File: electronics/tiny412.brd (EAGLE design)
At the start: 18.8 x 16.3 mm, 25 parts

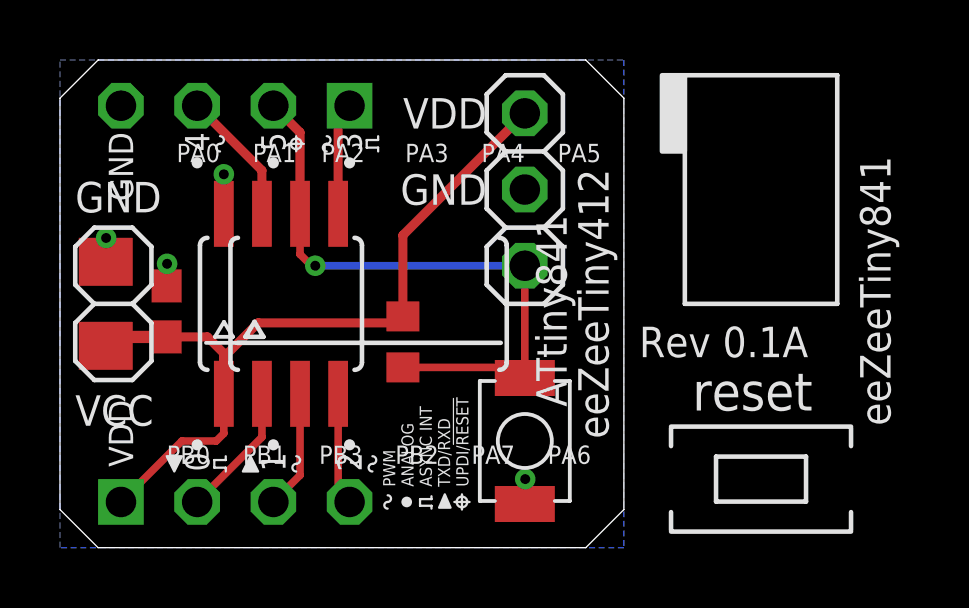
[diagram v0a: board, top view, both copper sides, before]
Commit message: Updated silk symbols, enlarged; fixed reset ckt, added HF filter cap
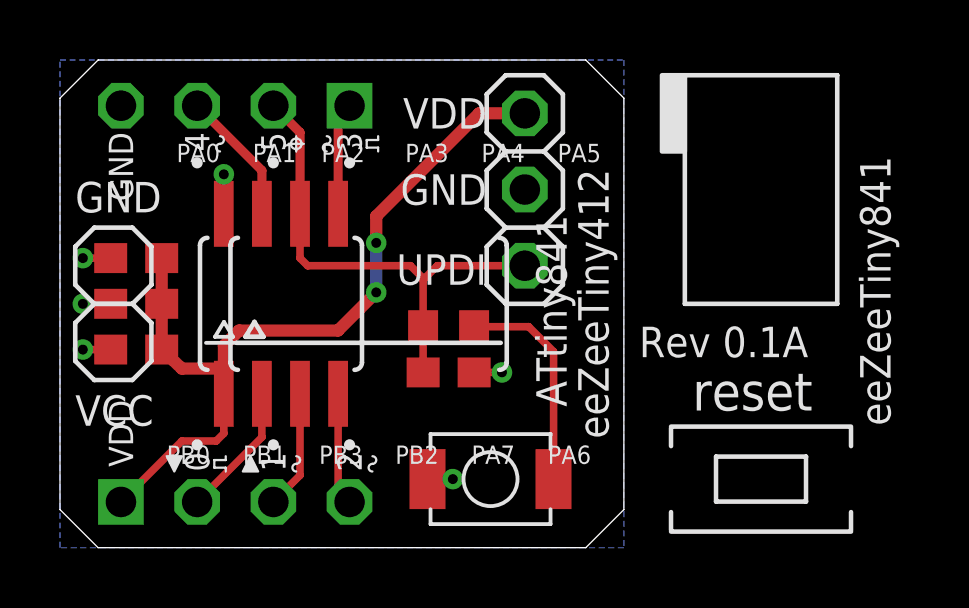
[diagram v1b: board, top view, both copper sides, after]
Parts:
- removed R1: 10k, rcl:R0603
- added C3: 102, rcl:C0603
- added C4: 104, rcl:C0603
- added R2: 330, rcl:R0603
- C2: device bt_rcl:1206 -> bt_rcl:0603
- S1: value RST -> RESET
- moved U$10 5.64 mm to (17.4, 4.19), flipped to the bottom, turned to 0 degrees
- moved C2 1.83 mm to (2.54, 9.65), turned to 180 degrees
- moved U$1 1.78 mm to (5.84, 6.73)
- moved S1 1.71 mm to (14.4, 2.29), turned to 0 degrees
- moved C1 1.63 mm to (2.54, 6.60), turned to 180 degrees
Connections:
- new net N$1: R2.1, S1.P$2
- net !RESET: now also C4.1, R2.2; no longer R1.1, S1.P$2
- net GND: now also C3.2, C4.2
- net VCC: now also C3.1; no longer R1.2
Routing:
- net N$1: track 0.00 -> 7.24 mm
- net !RESET: track 21.0 -> 16.6 mm, vias 1 -> 0
- net GND: track 3.68 -> 5.87 mm, vias 4 -> 6
- net VCC: track 28.1 -> 27.4 mm, vias 0 -> 2
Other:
- board text added: "R0.2"
- board text added: "cc-by-sa"
- board text removed: "CC-BY-SA"
- board text removed: "R0.1"

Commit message: remove reset, updated pin desc, added doc url
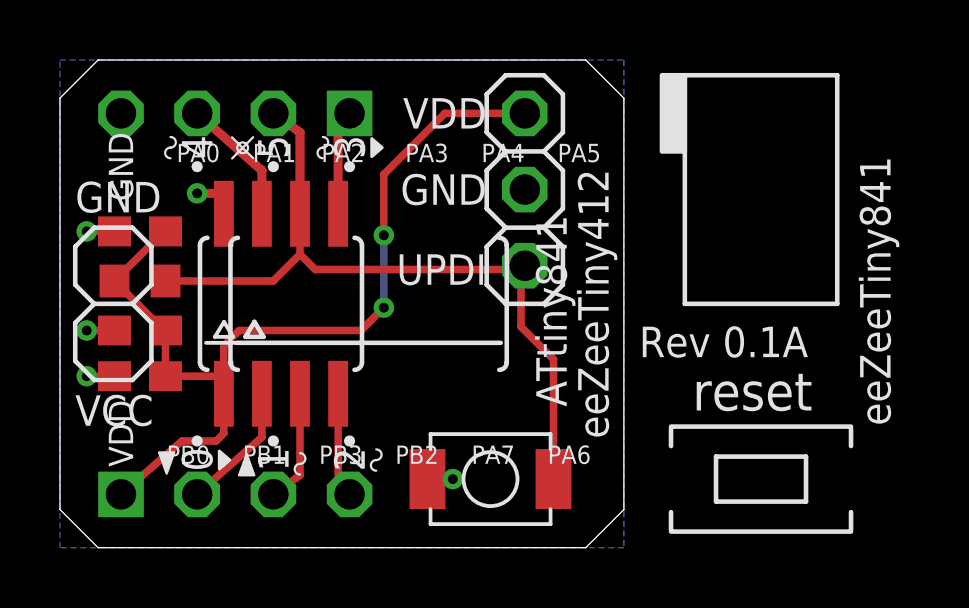
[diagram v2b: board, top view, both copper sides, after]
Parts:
- removed C4: 104, rcl:C0603
- R2: value 330 -> 10k
- moved R2 10.4 mm to (2.67, 8.89)
- moved U$11 1.78 mm to (6.10, 13.3)
- moved U$3 1.66 mm to (3.68, 13.3)
- moved C2 0.90 mm to (2.67, 10.5)
- moved C1 0.90 mm to (2.67, 5.71)
- moved C3 0.90 mm to (2.67, 7.24)
- moved U$9 0.28 mm to (3.56, 2.92)
- moved JP1 0.25 mm to (5.84, 1.78)
- moved JP3 0.25 mm to (5.84, 14.5)
- moved U$1 0.25 mm to (5.84, 6.48)
- moved U$5 0.18 mm to (5.46, 2.92)
- moved U$7 0.18 mm to (10.5, 2.92)
- moved U$8 0.18 mm to (6.22, 2.67)
- moved U$2 0.18 mm to (8.76, 13.3)
- moved U$4 0.18 mm to (10.5, 13.3)
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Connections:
- removed net N$1: R2.1, S1.P$2
- net !RESET: now also R2.1, S1.P$2; no longer C4.1, R2.2
- net GND: no longer C4.2
- net VCC: now also R2.2
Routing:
- net !RESET: track 16.6 -> 25.2 mm
- net N$1: track 7.24 -> 0.00 mm
- net VCC: track 27.4 -> 31.7 mm
- net GND: track 5.87 -> 5.13 mm, vias 6 -> 5
